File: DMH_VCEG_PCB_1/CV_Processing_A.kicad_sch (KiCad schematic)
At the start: 59 parts, among them J25 Conn_01x10_PinHeader, Q3 BC558, Q4 BC558, Q5 BC548, Q6 BC548, Q7 BC548, Q8 BC548, U10 TL074, U5 TL074, U7 TL074, U9 TL074

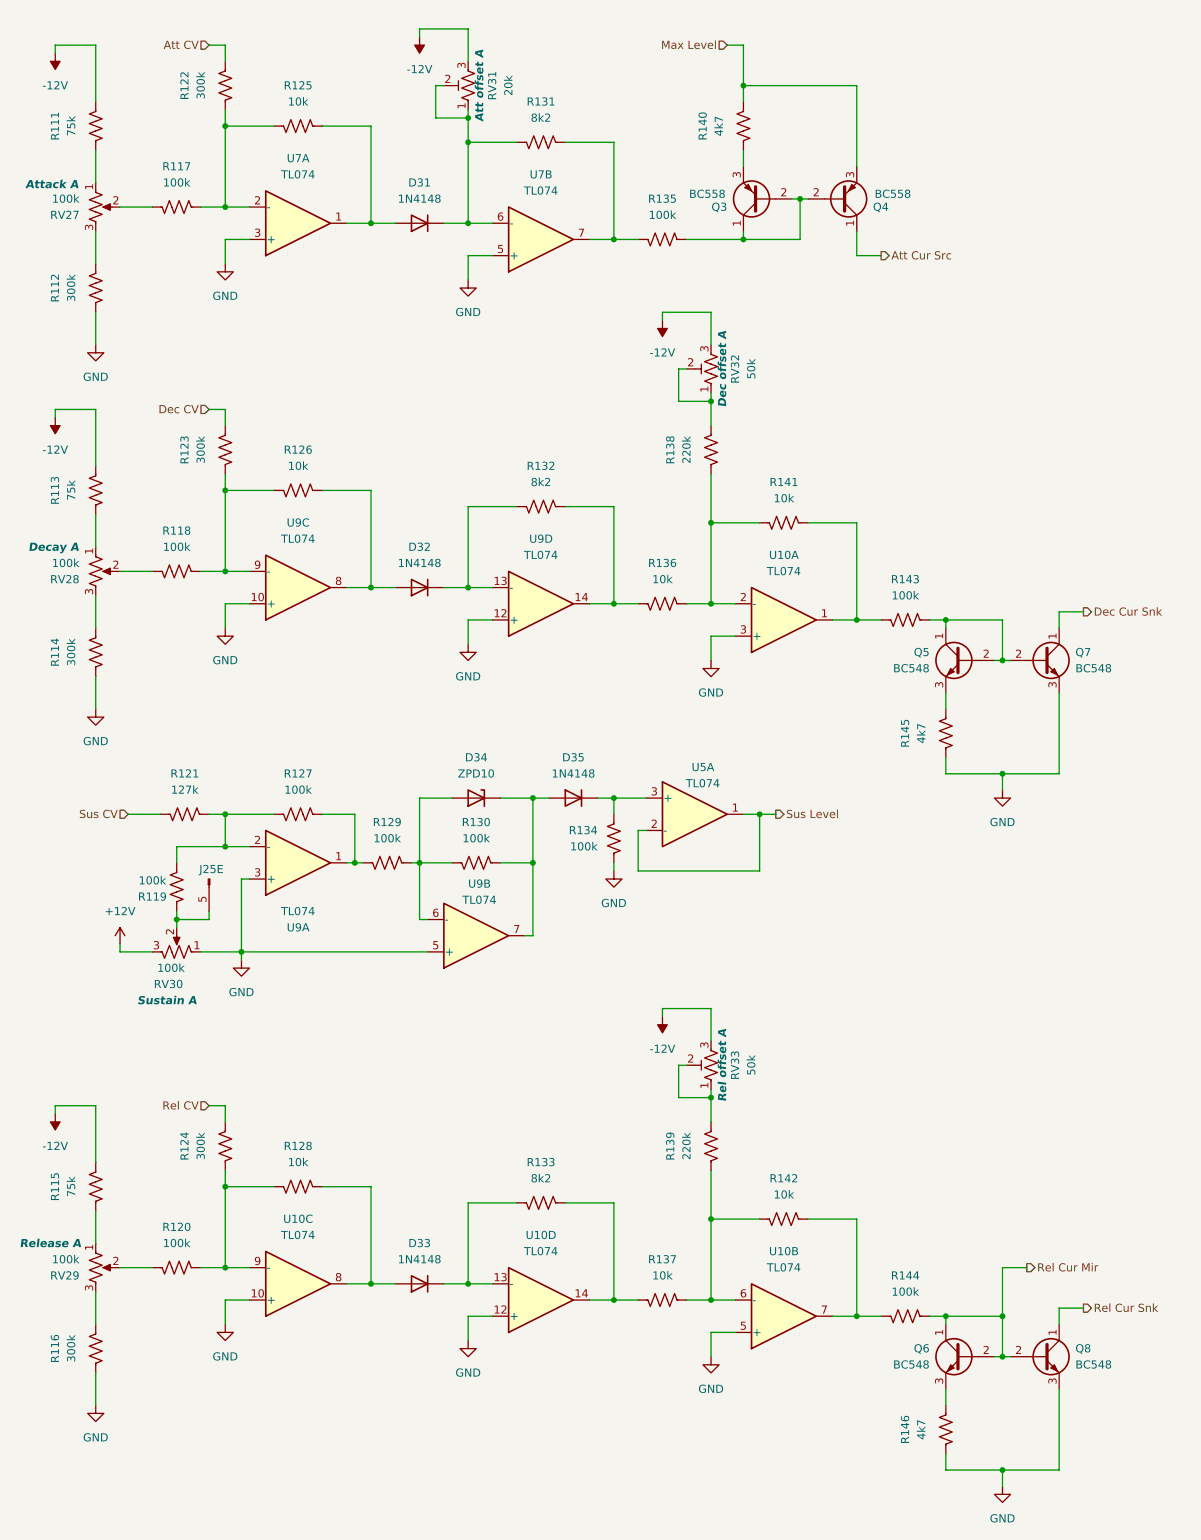
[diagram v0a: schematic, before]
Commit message: Divided components between PCB 1 and 2
Still need to:
- Place interface pins where needed
- Set "exclude from board" options where needed
- Copy schematic over to PCB 2 project
- Invert "exclude from board" options where needed
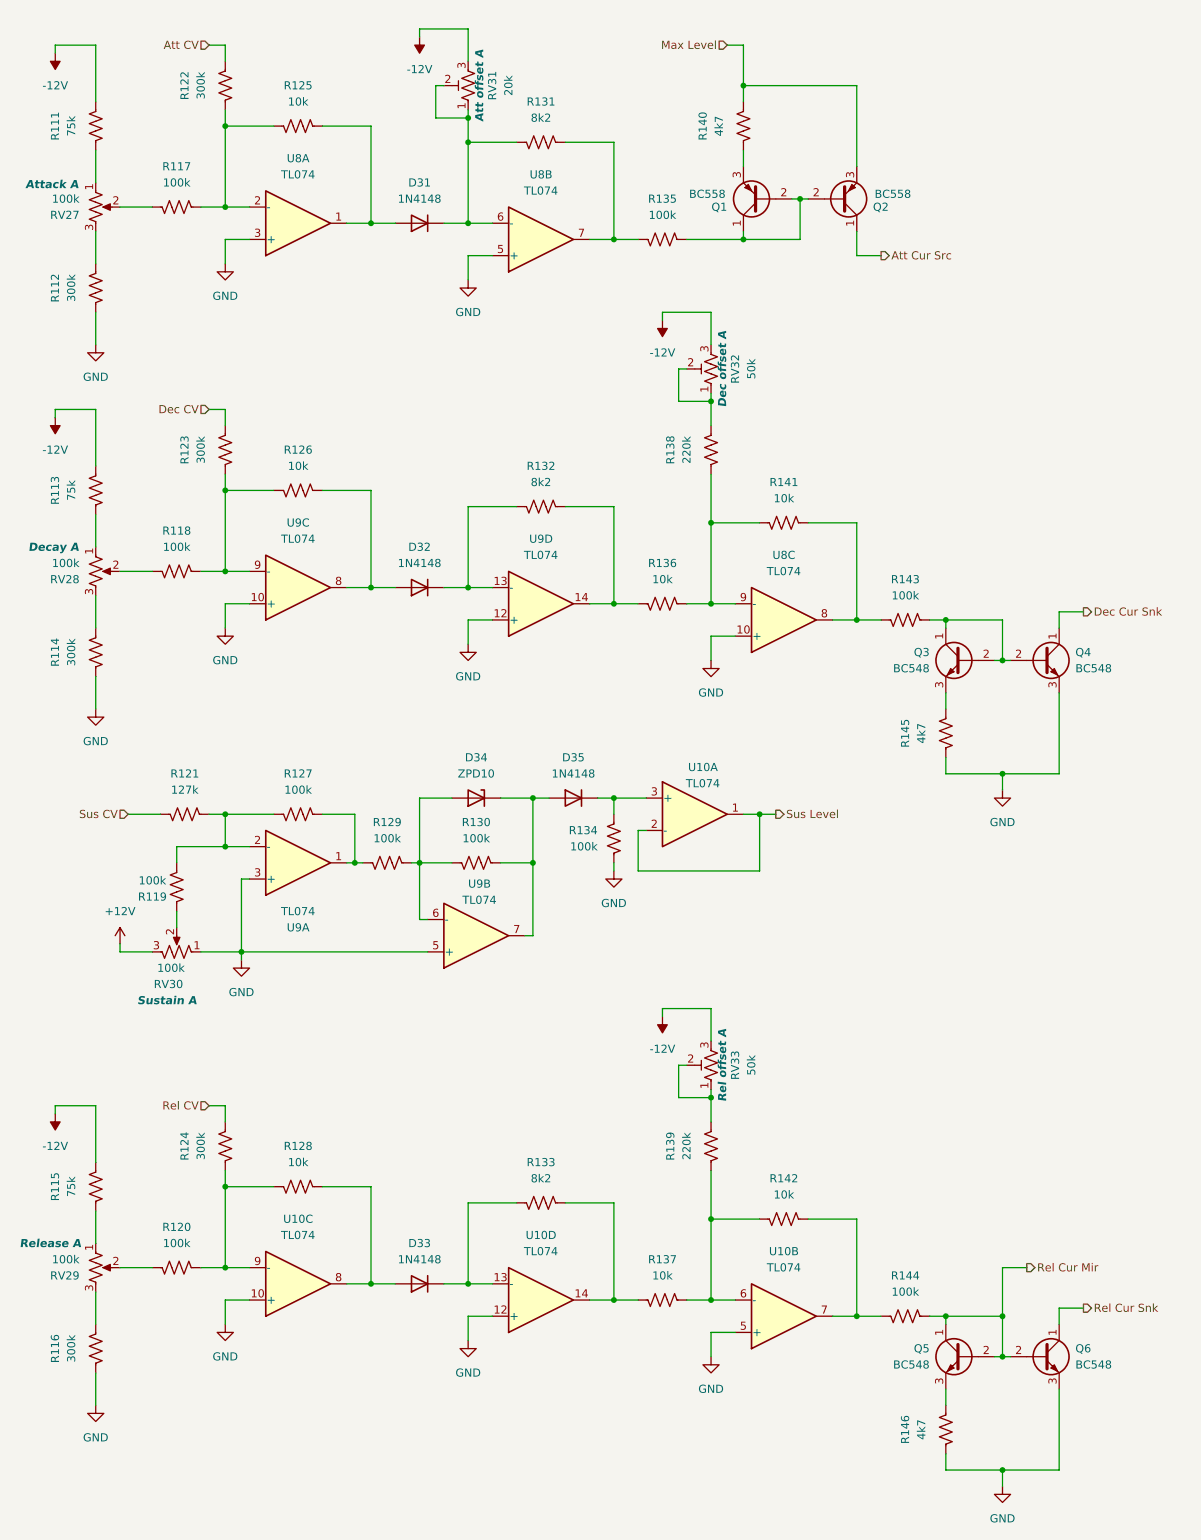
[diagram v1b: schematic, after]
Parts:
- removed J25: Conn_01x10_PinHeader, symbol SynthStuff:Conn_01x10_PinHeader
- renumbered Q3 to Q1, Q4 to Q2, Q5 to Q3, Q7 to Q4, Q6 to Q5, Q8 to Q6, U5 to U10, U7 to U8, U10 to U8
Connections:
- net GND: now also U8.10 (+); no longer U8.3 (+)
- net at R136.2, R138.1, R141.1: now also U8.9 (-); no longer U8.2 (-)
- net at R141.2, R143.1: now also U8.8; no longer U8.1
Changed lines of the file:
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@@
 	)
 	(junction
-		(at 38.1 156.21)
-		(diameter 0)
-		(color 0 0 0 0)
-	)
-	(junction
 		(at 45.72 101.6)
 		(diameter 0)
@@
 	(wire
 		(pts
-			(xy 38.1 156.21) (xy 38.1 157.48)
+			(xy 38.1 154.94) (xy 38.1 157.48)
 		)
 		(stroke
@@
 	(wire
 		(pts
-			(xy 38.1 154.94) (xy 38.1 156.21)
-		)
-		(stroke
-			(width 0)
-			(type default)
-		)
-	)
-	(wire
-		(pts
 			(xy 137.16 203.2) (xy 144.78 203.2)
 		)
@@
 	(wire
 		(pts
-			(xy 43.18 154.94) (xy 43.18 156.21)
-		)
-		(stroke
-			(width 0)
-			(type default)
-		)
-	)
-	(wire
-		(pts
 			(xy 114.3 60.96) (xy 121.92 60.96)
 		)
@@
 	(wire
 		(pts
-			(xy 43.18 156.21) (xy 38.1 156.21)
-		)
-		(stroke
-			(width 0)
-			(type default)
-		)
-	)
-	(wire
-		(pts
 			(xy 83.82 46.99) (xy 87.63 46.99)
 		)
@@
 		(on_board yes)
 		(dnp no)
-		(property "Reference" "Q6"
+		(property "Reference" "Q5"
 			(at 156.21 223.5199 0)
 			(effects
@@
 			(project "DMH_VCEG_PCB_1"
 				(path "/58f4306d-5387-4983-bb08-41a2313fd315/7d3cb848-7f4a-41b7-b3df-5bb0c19476ef"
-					(reference "Q6")
+					(reference "Q5")
 					(unit 1)
 				)
@@
 		(on_board yes)
 		(dnp no)
-		(property "Reference" "Q3"
+		(property "Reference" "Q1"
 			(at 124.46 44.4501 0)
 			(effects
@@
 			(project "DMH_VCEG_PCB_1"
 				(path "/58f4306d-5387-4983-bb08-41a2313fd315/7d3cb848-7f4a-41b7-b3df-5bb0c19476ef"
-					(reference "Q3")
+					(reference "Q1")
 					(unit 1)
 				)
@@
 		(on_board yes)
 		(dnp no)
-		(property "Reference" "U5"
+		(property "Reference" "U10"
 			(at 120.65 132.334 0)
 			(effects
@@
 			(project "DMH_VCEG_PCB_1"
 				(path "/58f4306d-5387-4983-bb08-41a2313fd315/7d3cb848-7f4a-41b7-b3df-5bb0c19476ef"
-					(reference "U5")
+					(reference "U10")
 					(unit 1)
 				)
@@
 		(exclude_from_sim no)
 		(in_bom yes)
-		(on_board yes)
+		(on_board no)
 		(dnp no)
 		(fields_autoplaced yes)
-		(property "Reference" "U7"
+		(property "Reference" "U8"
 			(at 95.25 39.37 0)
 			(effects
@@
 			(project ""
 				(path "/58f4306d-5387-4983-bb08-41a2313fd315/7d3cb848-7f4a-41b7-b3df-5bb0c19476ef"
-					(reference "U7")
+					(reference "U8")
 					(unit 2)
 				)
@@
 		(exclude_from_sim no)
 		(in_bom yes)
-		(on_board yes)
+		(on_board no)
 		(dnp no)
 		(fields_autoplaced yes)
-		(property "Reference" "U7"
+		(property "Reference" "U8"
 			(at 57.15 36.83 0)
 			(effects
@@
 			(project ""
 				(path "/58f4306d-5387-4983-bb08-41a2313fd315/7d3cb848-7f4a-41b7-b3df-5bb0c19476ef"
-					(reference "U7")
+					(reference "U8")
 					(unit 1)
 				)
@@
 		(on_board yes)
 		(dnp no)
-		(property "Reference" "Q4"
+		(property "Reference" "Q2"
 			(at 147.32 44.4501 0)
 			(effects
@@
 			(project "DMH_VCEG_PCB_1"
 				(path "/58f4306d-5387-4983-bb08-41a2313fd315/7d3cb848-7f4a-41b7-b3df-5bb0c19476ef"
-					(reference "Q4")
+					(reference "Q2")
 					(unit 1)
 				)
@@
 		(at 133.35 109.22 0)
 		(mirror x)
-		(unit 1)
+		(unit 3)
 		(exclude_from_sim no)
 		(in_bom yes)
-		(on_board yes)
+		(on_board no)
 		(dnp no)
 		(fields_autoplaced yes)
-		(property "Reference" "U10"
+		(property "Reference" "U8"
 			(at 133.35 99.06 0)
 			(effects
@@
 			(project ""
 				(path "/58f4306d-5387-4983-bb08-41a2313fd315/7d3cb848-7f4a-41b7-b3df-5bb0c19476ef"
-					(reference "U10")
-					(unit 1)
+					(reference "U8")
+					(unit 3)
 				)
 			)
@@
 		(on_board yes)
 		(dnp no)
-		(property "Reference" "Q7"
+		(property "Reference" "Q4"
 			(at 179.07 114.2999 0)
 			(effects
@@
 			(project "DMH_VCEG_PCB_1"
 				(path "/58f4306d-5387-4983-bb08-41a2313fd315/7d3cb848-7f4a-41b7-b3df-5bb0c19476ef"
-					(reference "Q7")
+					(reference "Q4")
 					(unit 1)
 				)
@@
 		(on_board yes)
 		(dnp no)
-		(property "Reference" "Q5"
+		(property "Reference" "Q3"
 			(at 156.21 114.2999 0)
 			(effects
@@
 			(project "DMH_VCEG_PCB_1"
 				(path "/58f4306d-5387-4983-bb08-41a2313fd315/7d3cb848-7f4a-41b7-b3df-5bb0c19476ef"
-					(reference "Q5")
+					(reference "Q3")
 					(unit 1)
 				)
@@
 		(on_board yes)
 		(dnp no)
-		(property "Reference" "Q8"
+		(property "Reference" "Q6"
 			(at 179.07 223.5199 0)
 			(effects
@@
 			(project "DMH_VCEG_PCB_1"
 				(path "/58f4306d-5387-4983-bb08-41a2313fd315/7d3cb848-7f4a-41b7-b3df-5bb0c19476ef"
-					(reference "Q8")
+					(reference "Q6")
 					(unit 1)
 				)
@@
 				)
 			)
-		)
-	)
-	(symbol
-		(lib_id "SynthStuff:Conn_01x10_PinHeader")
-		(at 43.18 149.86 90)
-		(mirror x)
-		(unit 5)
-		(exclude_from_sim no)
-		(in_bom yes)
-		(on_board yes)
-		(dnp no)
-		(property "Reference" "J25"
-			(at 45.466 148.336 90)
-			(effects
-				(font
-					(size 1.27 1.27)
-				)
-				(justify left)
-			)
-		)
-		(property "Value" "Conn_01x10_PinHeader"
-			(at 45.72 149.86 0)
-			(effects
-				(font
-					(size 1.27 1.27)
-				)
-				(hide yes)
-			)
-		)
-		(property "Footprint" ""
-			(at 43.18 149.86 0)
-			(effects
-				(font
-					(size 1.27 1.27)
-				)
-				(hide yes)
-			)
-		)
-		(property "Datasheet" "~"
-			(at 43.18 149.86 0)
-			(effects
-				(font
-					(size 1.27 1.27)
-				)
-				(hide yes)
-			)
-		)
-		(property "Description" "Generic connector, single row, 01x10"
-			(at 43.18 149.86 0)
-			(effects
-				(font
-					(size 1.27 1.27)
-				)
-				(hide yes)
-			)
-		)
-		(pin "10"
-		)
-		(pin "4"
-		)
-		(pin "8"
-		)
-		(pin "3"
-		)
-		(pin "7"
-		)
-		(pin "6"
-		)
-		(pin "9"
-		)
-		(pin "5"
-		)
-		(pin "1"
-		)
-		(pin "2"
-		)
-		(instances
-			(project "DMH_VCEG_PCB_1"
-				(path "/58f4306d-5387-4983-bb08-41a2313fd315/7d3cb848-7f4a-41b7-b3df-5bb0c19476ef"
-					(reference "J25")
-					(unit 5)
-				)
-			)

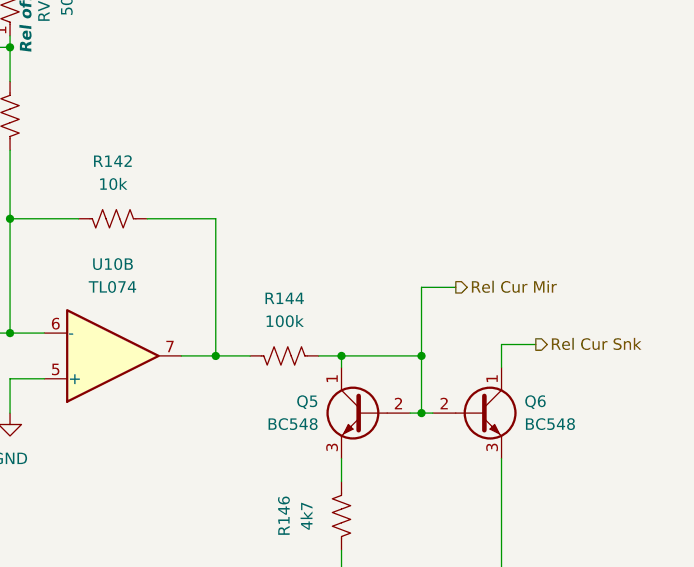
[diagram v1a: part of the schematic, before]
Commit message: Reworked Out R A circuit
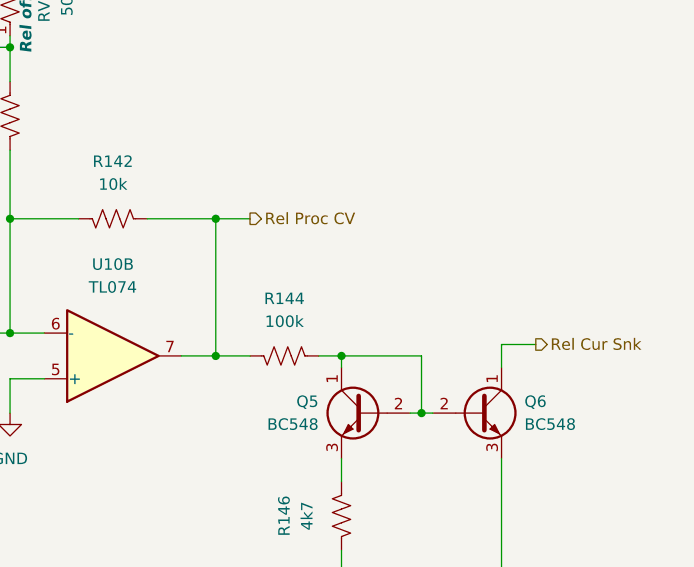
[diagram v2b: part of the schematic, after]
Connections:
- net Rel Proc CV: now reaches R142.2, R144.1, U10.7
- net Rel Cur Mir: no longer names the net of Q5.1 (C), Q5.2 (B), Q6.2 (B), R144.2
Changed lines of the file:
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@@
-	)
-	(junction
-		(at 167.64 218.44)
-		(diameter 0)
-		(color 0 0 0 0)
 	)
 	(junction
@@
 	)
 	(junction
+		(at 144.78 203.2)
+		(diameter 0)
+		(color 0 0 0 0)
+	)
+	(junction
 		(at 158.75 109.22)
 		(diameter 0)
@@
 	(wire
 		(pts
-			(xy 171.45 210.82) (xy 167.64 210.82)
+			(xy 148.59 203.2) (xy 144.78 203.2)
 		)
 		(stroke
@@
 		(pts
 			(xy 48.26 161.29) (xy 48.26 162.56)
-		)
-		(stroke
-			(width 0)
-			(type default)
-		)
-	)
-	(wire
-		(pts
-			(xy 167.64 210.82) (xy 167.64 218.44)
 		)
 		(stroke
@@
 		)
 	)
-	(hierarchical_label "Rel Cur Mir"
+	(hierarchical_label "Rel Proc CV"
 		(shape output)
-		(at 171.45 210.82 0)
+		(at 148.59 203.2 0)
 		(effects
 			(font
